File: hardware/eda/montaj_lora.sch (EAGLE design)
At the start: 6 parts, among them U1 RA-02_LORA, X1 MINI-USB-SHIELD-UX60-MB-5S8

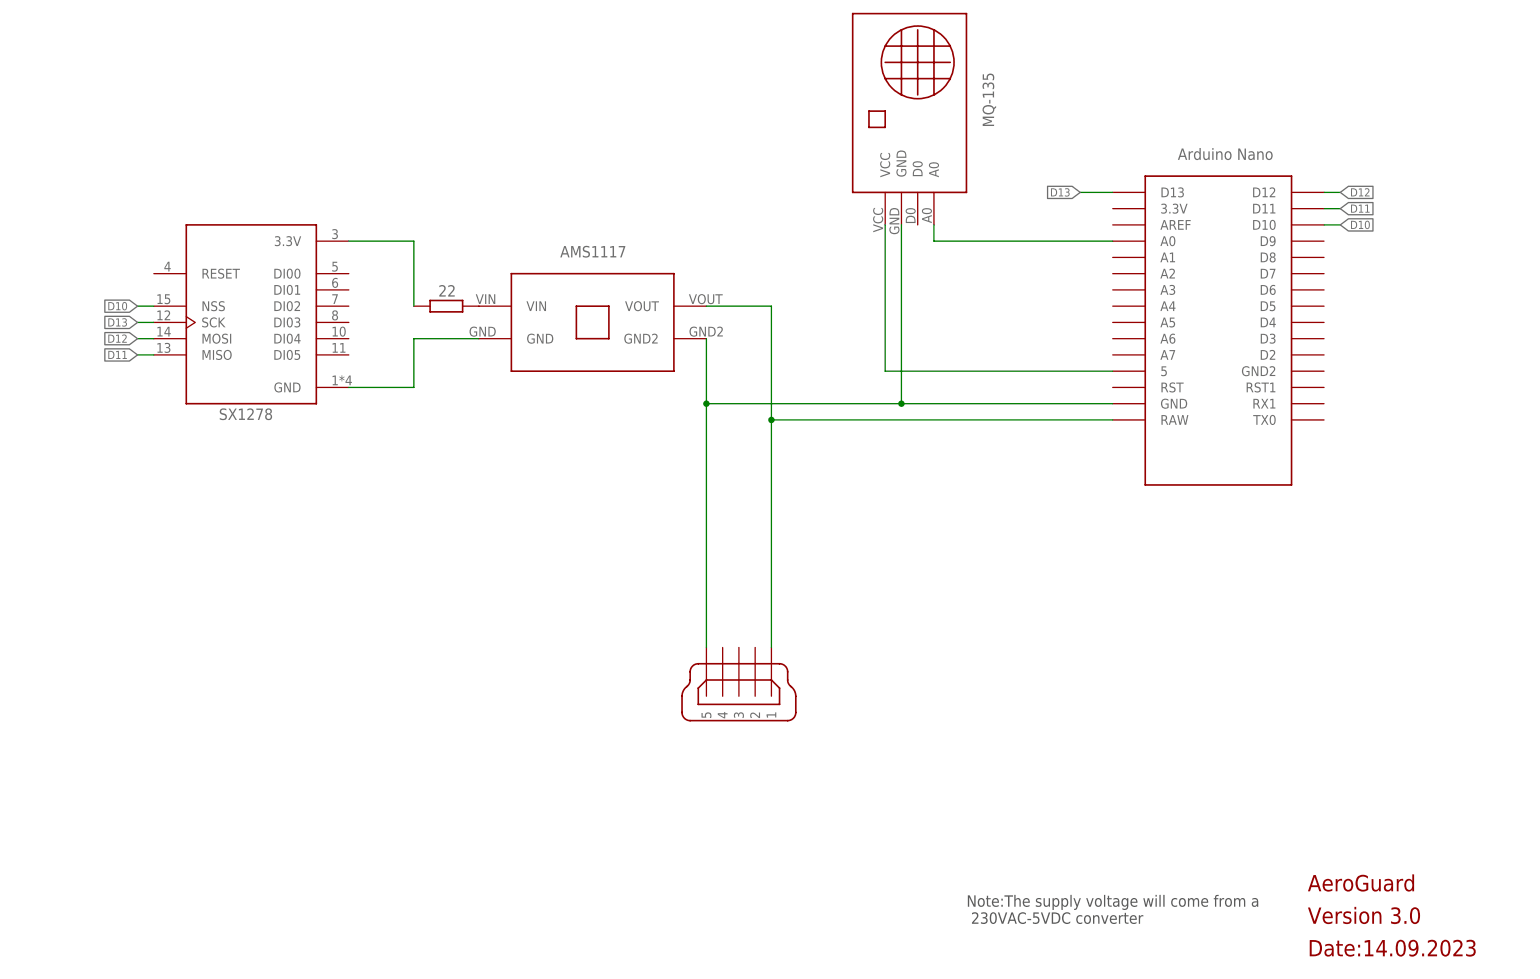
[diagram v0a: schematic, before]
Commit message: Adaugare modul DHT11
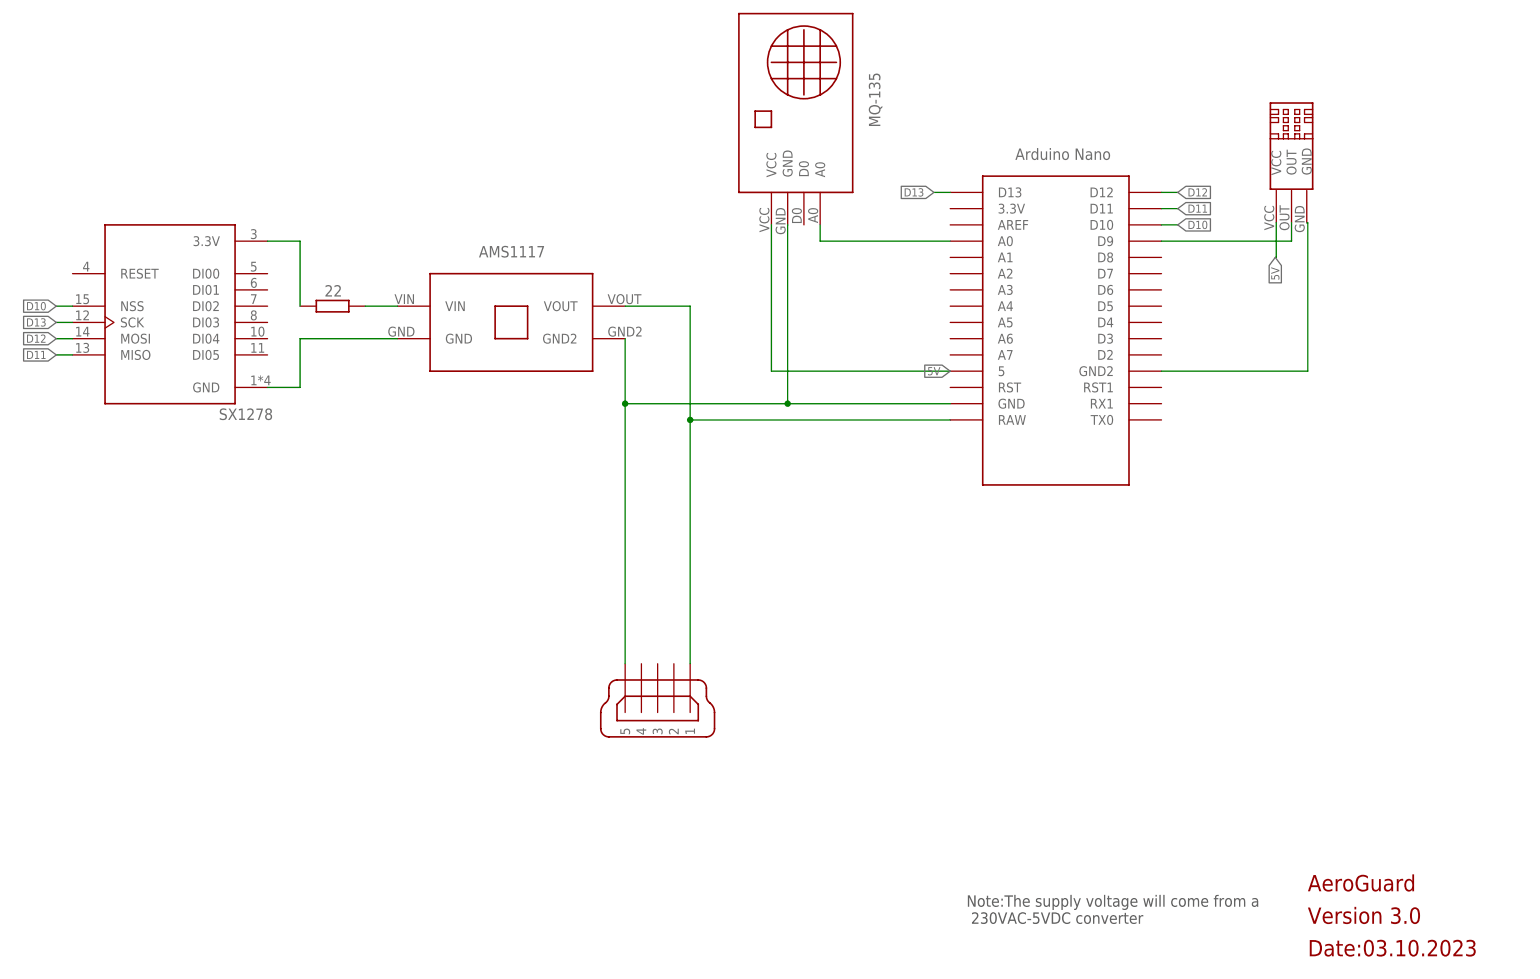
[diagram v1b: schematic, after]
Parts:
- added U$4: DHT11, componente:DHT11
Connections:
- net N$4 renamed 5V
- new net N$3: U$4.VCC
- new net N$8: U$1.D9, U$4.OUT
- new net N$9: U$1.GND2, U$4.GND
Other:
- note added: "Date:03.10.2023"
- note removed: "Date:14.09.2023"
- moved on the sheet: 22
